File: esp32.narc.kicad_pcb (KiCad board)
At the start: 2 copper layers, 1 part, among them U0 CUSTOM-ESP32-PICO-D4

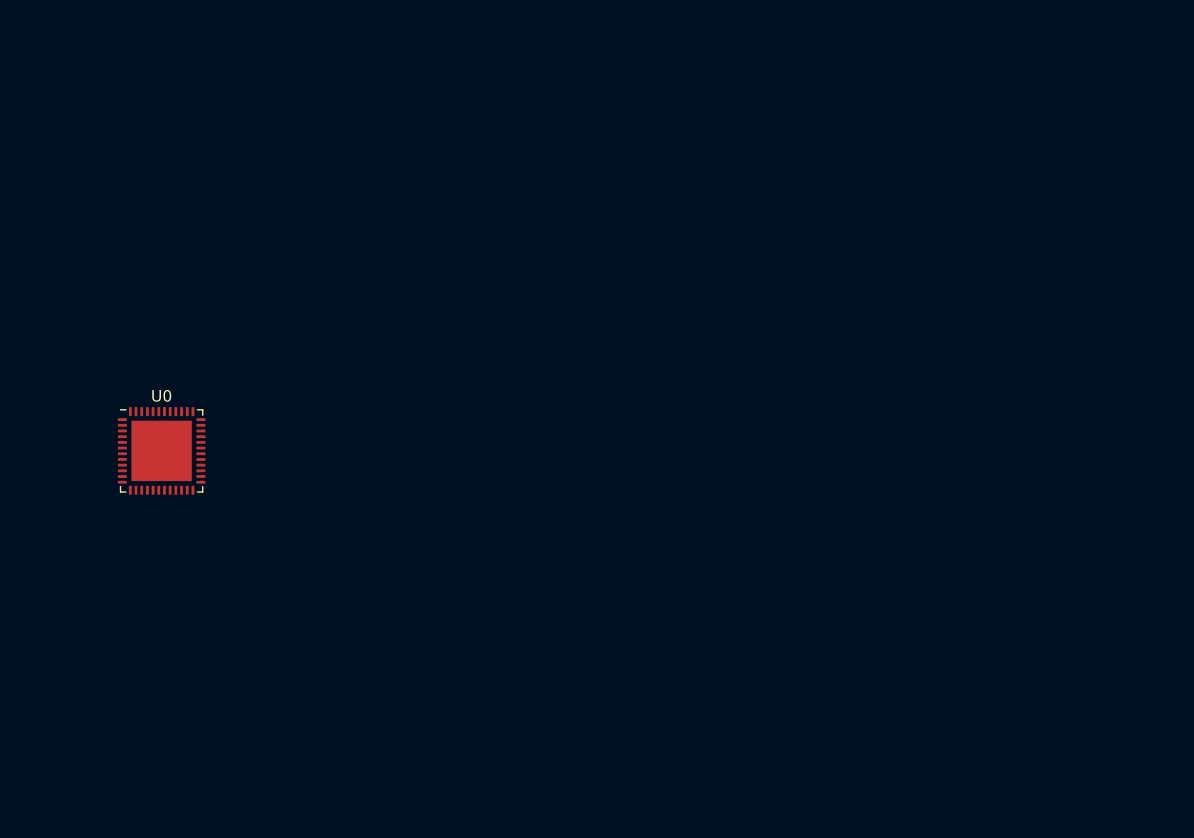
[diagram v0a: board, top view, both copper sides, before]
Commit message: Update footprints
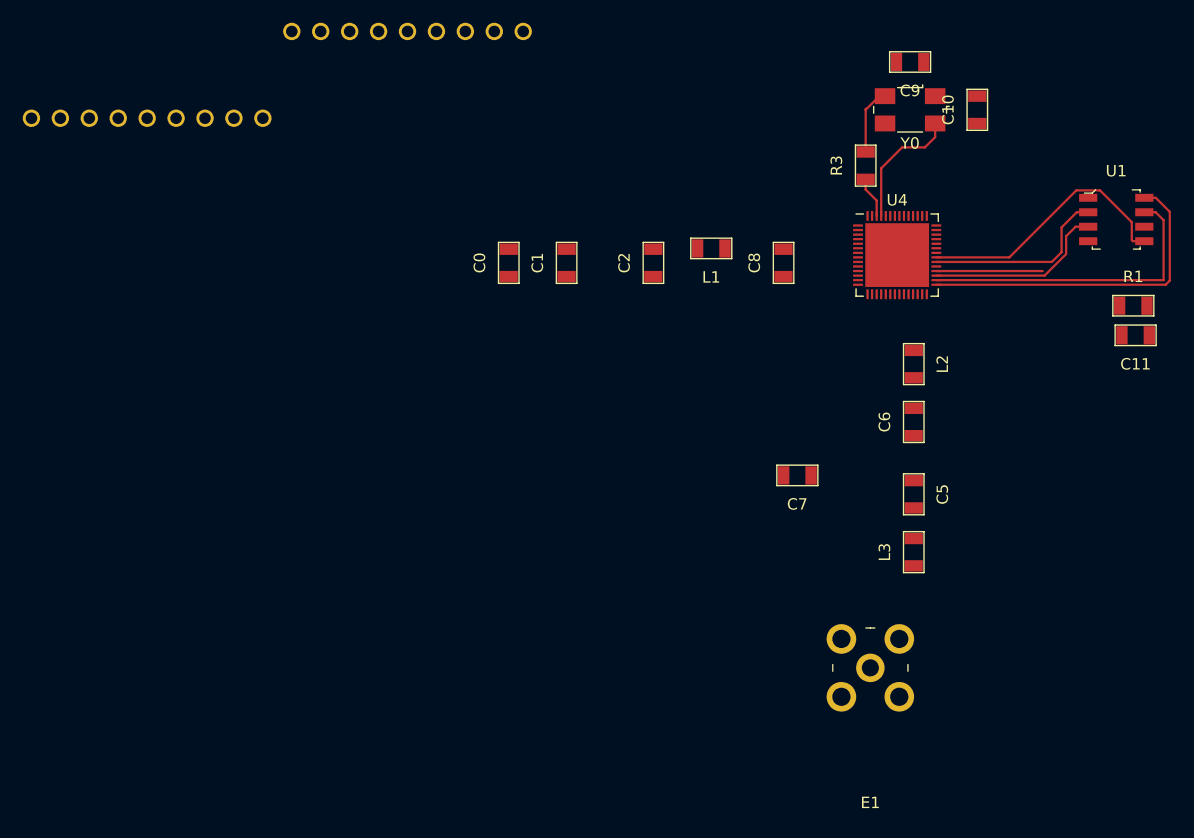
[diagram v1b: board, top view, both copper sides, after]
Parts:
- removed U0: CUSTOM-ESP32-PICO-D4, Package_DFN_QFN:QFN-48-1EP_7x7mm_P0.5mm_EP5.3x5.3mm
- added C0: 10uF, esp32narc:cap_3.20x1.60mm, F.Cu at (124.5, 91.4)
- added C1: 1uF, esp32narc:cap_3.20x1.60mm, F.Cu at (129.5, 91.4)
- added C10: C, esp32narc:cap_3.20x1.60mm, F.Cu at (165.6, 78.0)
- added C11: 0.1uF, esp32narc:cap_3.20x1.60mm, F.Cu at (179.5, 97.8)
- added C2: 0.1uF, esp32narc:cap_3.20x1.60mm, F.Cu at (137.2, 91.4)
- added C5: C_Small, esp32narc:cap_3.20x1.60mm, F.Cu at (160.0, 111.8)
- added C6: C_Small, esp32narc:cap_3.20x1.60mm, F.Cu at (160.0, 105.4)
- added C7: C_Small, esp32narc:cap_3.20x1.60mm, F.Cu at (149.8, 110.1)
- added C8: C_Small, esp32narc:cap_3.20x1.60mm, F.Cu at (148.6, 91.4)
- added C9: C, esp32narc:cap_3.20x1.60mm, F.Cu at (159.7, 73.8)
- added E1: PRO-OB-440, DIGIKEY:RF_SMA_RightAngle_5-1814400-1, F.Cu at (156.2, 127.0)
- added L1: L_Small, esp32narc:cap_3.20x1.60mm, F.Cu at (142.2, 90.2)
- added L2: L_Small, esp32narc:cap_3.20x1.60mm, F.Cu at (160.0, 100.3)
- added L3: L_Small, esp32narc:cap_3.20x1.60mm, F.Cu at (160.0, 116.8)
- added LE_HEADERS1: PINHEAD9, esp32narc:PINHEAD9, F.Cu at (91.4, 78.7)
- added R1: 100K, esp32narc:cap_3.20x1.60mm, F.Cu at (179.3, 95.2)
- added R3: R_Small_US, esp32narc:cap_3.20x1.60mm, F.Cu at (155.8, 82.9)
- added RE_HEADERS1: PINHEAD9, esp32narc:PINHEAD9, F.Cu at (114.3, 71.1)
- added U1: W25Q32JVSSIQ_TR, DIGIKEY:SOIC-8_W5.3mm, F.Cu at (177.8, 87.6)
- added U4: ESP32-S3, esp32narc:ESP32-S3-SoC, F.Cu at (158.6, 90.8)
- added Y0: Crystal_GND24_Small, Crystal:Crystal_SMD_0603-4Pin_6.0x3.5mm, F.Cu at (159.7, 78.0)
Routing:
- net Net-(C11-Pad2): track 0.00 -> 29.4 mm
- net Net-(U1-Pad7): track 0.00 -> 27.2 mm
- net Net-(U1-Pad5): track 0.00 -> 23.5 mm
- net Net-(U1-Pad2): track 0.00 -> 16.4 mm
- net Net-(U1-Pad3): track 0.00 -> 16.0 mm
- net Net-(C10-Pad2): track 0.00 -> 11.3 mm
- net Net-(R1-Pad2): track 0.00 -> 9.34 mm
- net Net-(C9-Pad1): track 0.00 -> 6.14 mm
- net Net-(R3-Pad2): track 0.00 -> 3.62 mm

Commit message: Add antenna and some routes
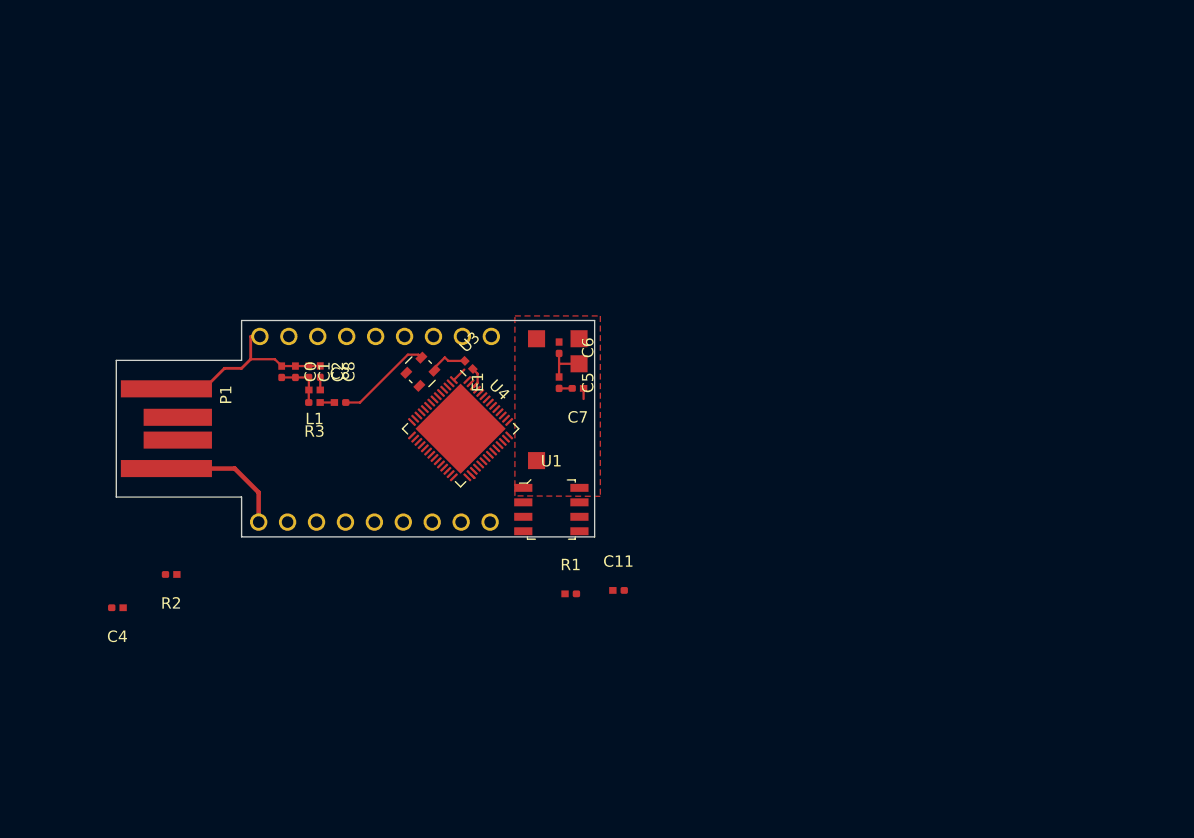
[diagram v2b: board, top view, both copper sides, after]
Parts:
- removed C10, C9: C, esp32narc:cap_3.20x1.60mm
- removed L2, L3: L_Small, esp32narc:cap_3.20x1.60mm
- removed Y0: Crystal_GND24_Small, Crystal:Crystal_SMD_0603-4Pin_6.0x3.5mm
- added C3: 0.1uF, esp32narc:cap_3.20x1.60mm, F.Cu at (109.7, 103.7)
- added C4: C_Small, esp32narc:cap_3.20x1.60mm, F.Cu at (90.1, 121.7)
- added L0: 10nH, esp32narc:L_3.20x1.60mm, F.Cu at (121.0, 100.4)
- added P1: usbpads, esp32narc:usbpads, F.Cu at (98.4, 106.0)
- added R2: R_Small_US, esp32narc:cap_3.20x1.60mm, F.Cu at (94.8, 118.8)
- added U3: 625L3C040M, esp32narc:625L3C040M00000, F.Cu at (116.7, 101.0)
- E1: footprint DIGIKEY:RF_SMA_RightAngle_5-1814400-1 -> esp32narc:PRO-OB-440
- L1: footprint esp32narc:cap_3.20x1.60mm -> esp32narc:L_3.20x1.60mm
- moved U1 55.8 mm to (128.2, 113.1)
- moved R1 55.5 mm to (129.9, 120.5)
- moved R3 52.7 mm to (107.4, 103.7), turned to 0 degrees
- moved C11 50.6 mm to (134.1, 120.2), turned to 180 degrees
- moved LE_HEADERS1 43.2 mm to (111.4, 114.2)
- moved C8 41.8 mm to (107.9, 101.0), turned to 90 degrees
- moved U4 41.3 mm to (120.2, 106.0), turned to 315 degrees
- moved E1 38.6 mm to (130.6, 98.1), turned to 270 degrees
- moved L1 37.0 mm to (107.4, 102.6)
- moved C5 32.6 mm to (128.9, 102.0)
- moved C6 31.8 mm to (128.9, 98.9), turned to 90 degrees
- moved C2 31.7 mm to (106.9, 101.0), turned to 90 degrees
- moved RE_HEADERS1 27.7 mm to (111.5, 97.9)
- moved C1 25.7 mm to (105.7, 101.0), turned to 90 degrees
- moved C0 22.1 mm to (104.5, 101.0), turned to 90 degrees
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- renumbered RE_HEADERS1 to LE_HEADERS1, LE_HEADERS1 to RE_HEADERS1
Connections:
- C5 pad 2: GNDREF -> Net-(C5-Pad2)
- C6 pad 1: Net-(C6-Pad1) -> Net-(C5-Pad2)
- C7 pad 1: Net-(C7-Pad1) -> Net-(C5-Pad1)
- E1 pad 1: (no net) -> GNDREF
- E1 pad 2: Net-(C6-Pad1) -> Net-(C5-Pad2)
- R3 pad 1: Net-(C9-Pad1) -> +3V3
- R3 pad 2: Net-(R3-Pad2) -> Net-(C3-Pad2)
- RE_HEADERS1 pad 1: (no net) -> GNDREF
- U1 pad 4: (no net) -> GNDREF
- U4 pad 1: Net-(C7-Pad1) -> Net-(C5-Pad1)
- U4 pad 49: (no net) -> Net-(P1-PadP2)
- U4 pad 50: (no net) -> Net-(P1-PadP3)
- U4 pad 53: Net-(C10-Pad2) -> (no net)
- U4 pad 54: Net-(R3-Pad2) -> Net-(L0-Pad2)
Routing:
- net Net-(C11-Pad2): track 29.4 -> 0.00 mm
- net Net-(U1-Pad7): track 27.2 -> 0.48 mm
- net Net-(U1-Pad5): track 23.5 -> 0.00 mm
- net GNDREF: track 0.00 -> 18.6 mm
- net Net-(U1-Pad2): track 16.4 -> 0.00 mm
- net Net-(U1-Pad3): track 16.0 -> 0.00 mm
- net (no net): track 0.00 -> 14.8 mm
- net Net-(C10-Pad2): track 11.3 -> 0.00 mm
- net Net-(R1-Pad2): track 9.34 -> 0.00 mm
- net Net-(C3-Pad1): track 0.00 -> 8.49 mm
- net Net-(C9-Pad1): track 6.14 -> 0.00 mm
- net +3V3: track 0.00 -> 4.59 mm
- net Net-(C5-Pad2): track 0.00 -> 3.82 mm
- net Net-(R3-Pad2): track 3.62 -> 0.00 mm
- net Net-(L0-Pad1): track 0.00 -> 3.42 mm
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- added copper zone on F.Cu, net GNDREF
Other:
- board outline added: 42 x 19 mm
- net class Default: clearance 0.2 -> 0.16; trace_width 0.25 -> 0.16
- rule trace_clearance: 0.2 -> 0.16
- rule trace_min: 0.2 -> 0.1
- rule via_min_size: 0.4 -> 0.2

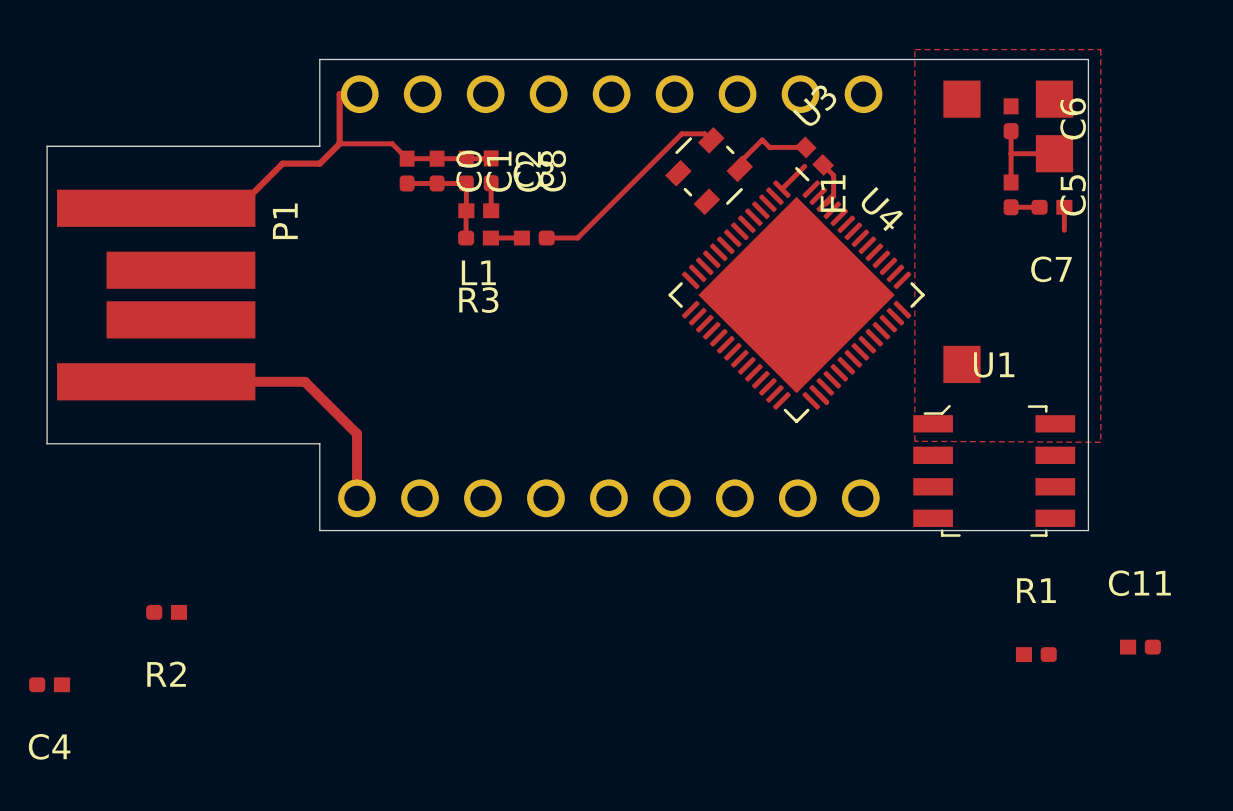
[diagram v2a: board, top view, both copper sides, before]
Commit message: added unrouted cp2102
considering cp2104 as well
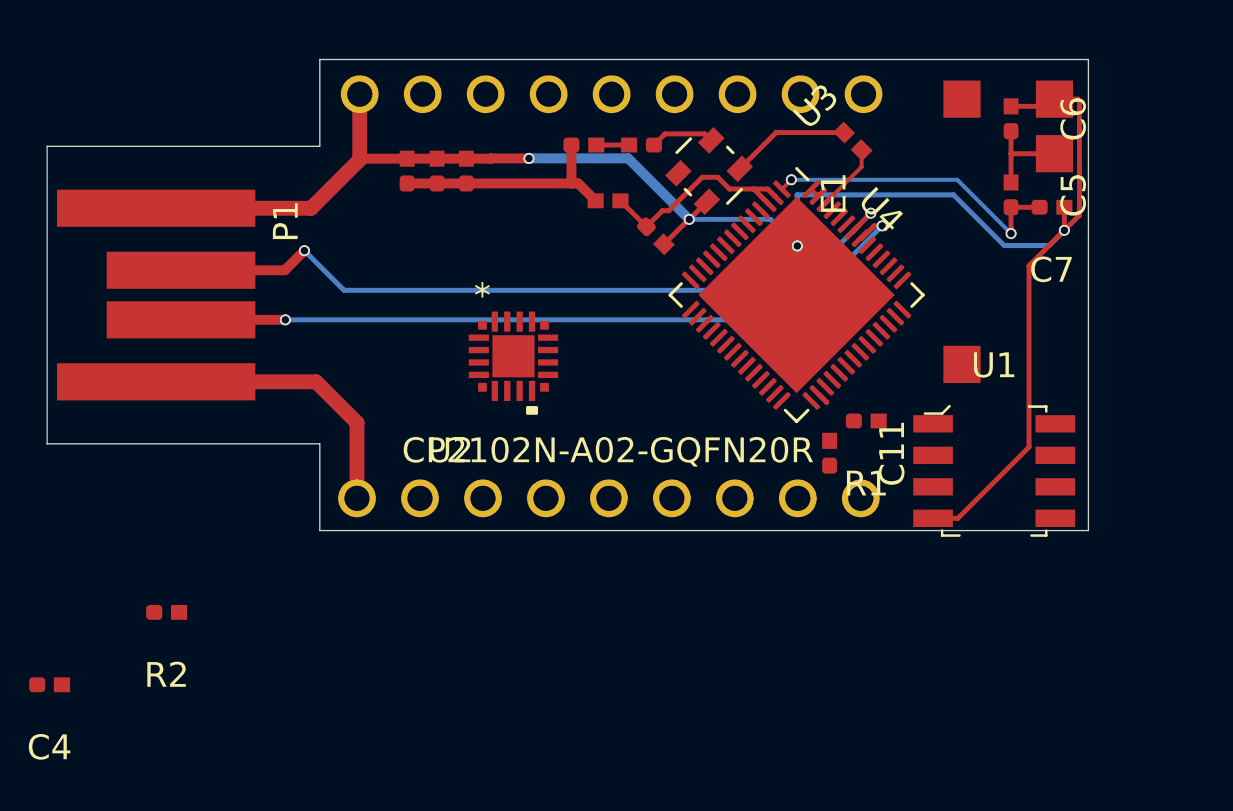
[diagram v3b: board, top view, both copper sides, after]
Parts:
- added U2: CP2102N-A02-GQFN20R, esp32narc:CP2102N-A02-GQFN20R, F.Cu at (108.8, 108.5)
- moved C11 14.8 mm to (121.6, 112.4), turned to 90 degrees
- moved R1 11.7 mm to (123.0, 111.1), turned to 0 degrees
- moved C8 7.11 mm to (114.5, 103.6), turned to 315 degrees
- moved C3 5.72 mm to (114.0, 100.0)
- moved R3 5.67 mm to (111.7, 100.0)
- moved L1 5.23 mm to (112.6, 102.2)
- moved L0 1.66 mm to (122.5, 99.8)
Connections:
- LE_HEADERS1 pad 1: (no net) -> +5V
- P1 pad P1: (no net) -> +5V
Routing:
- net GNDREF: track 18.6 -> 70.9 mm, vias 0 -> 4
- net Net-(P1-PadP3): track 0.00 -> 31.1 mm, vias 0 -> 2
- net Net-(P1-PadP2): track 0.00 -> 30.9 mm, vias 0 -> 2
- net (no net): track 14.8 -> 0.00 mm
- net +5V: track 0.00 -> 11.8 mm
- net Net-(C5-Pad1): track 2.45 -> 12.5 mm, vias 0 -> 2
- net Net-(C8-Pad1): track 1.11 -> 8.60 mm
- net Net-(C3-Pad1): track 8.49 -> 2.61 mm
- net +3V3: track 4.59 -> 9.44 mm
- net Net-(L0-Pad1): track 3.42 -> 4.82 mm
- net Net-(L0-Pad2): track 2.37 -> 3.23 mm
- removed copper zone on F.Cu, net GNDREF
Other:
- net class Default: via_dia 0.8 -> 0.45; via_drill 0.4 -> 0.3
